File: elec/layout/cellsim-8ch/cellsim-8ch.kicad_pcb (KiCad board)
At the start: 2 copper layers, 160 parts

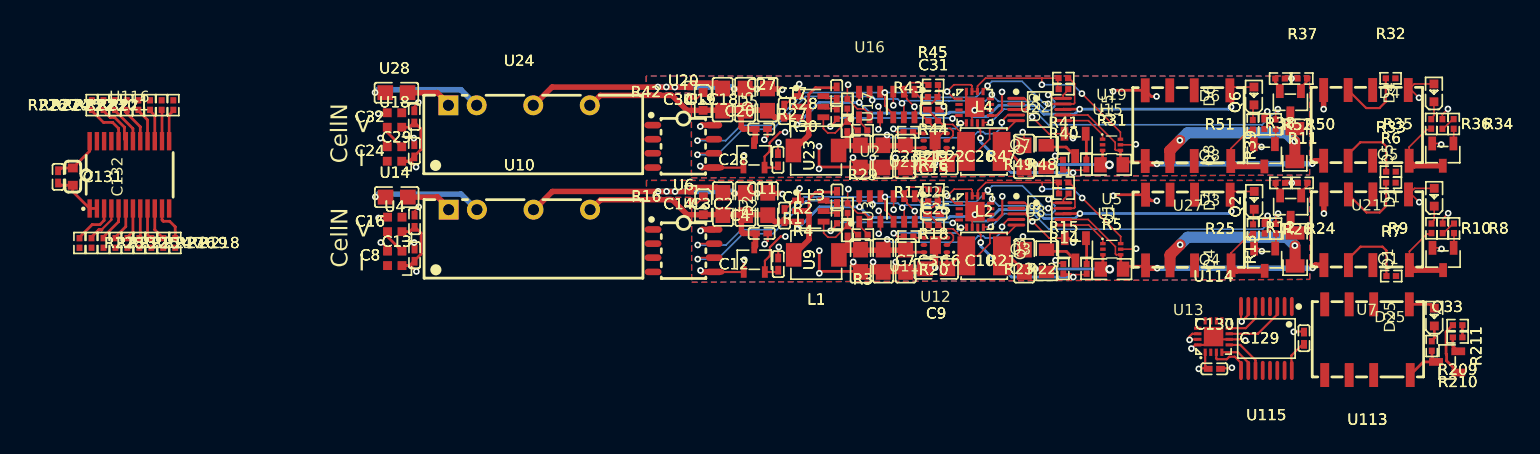
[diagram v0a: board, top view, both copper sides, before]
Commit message: remove muxes
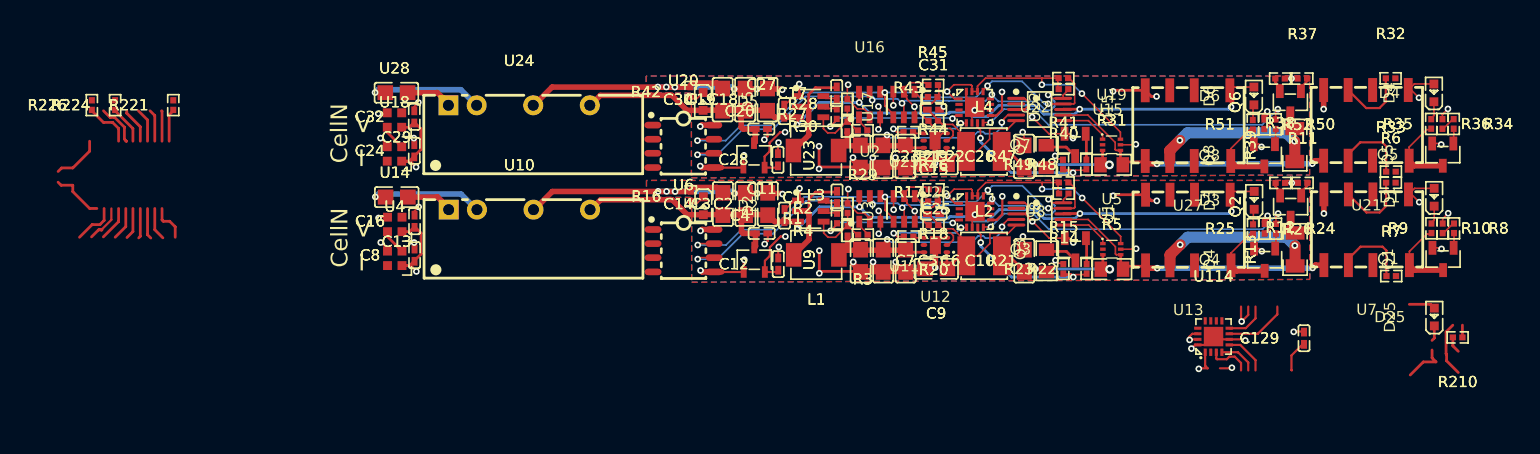
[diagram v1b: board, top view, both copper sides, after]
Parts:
- removed C130: 1µF ±10% 25V X5R, atopile:C0402-b3ef17
- removed C131: 100nF ±10% 16V X7R, atopile:C0402-b3ef17
- removed C132: 100nF ±10% 50V X7R, atopile:C0603-bd72f6
- removed Q33: , atopile:SOT-23-3_L2.9-W1.3-P1.90-LS2.4-BR-688f29
- removed R209, R212, R213, R214, R215, R216, R217, R218, R219, R220, R222, R223, R225, R227: 10kΩ ±1% 62.5mW, atopile:R0402-56259e
- removed R211, R228: 1kΩ ±1% 62.5mW, atopile:R0402-56259e
- removed U113: , lib:RELAY-SMD_HFD4-5-SR
- removed U115: , atopile:TSSOP-16_L5.0-W4.4-P0.65-LS6.4-BL-4f6acc
- removed U116: , lib:TSSOP-24_L7.8-W4.4-P0.65-LS6.4-BL
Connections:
- C10 pad 1: (no net) -> 3V3_GND
- C10 pad 2: 3V3_GND -> (no net)
- C11 pad 2: 3V3_GND -> (no net)
- C12 pad 2: 3V3_GND -> (no net)
- C129 pad 2: gnd-2 -> (no net)
- C13 pad 1: hv-4 -> hv-3
- C13 pad 2: gnd-3 -> gnd-1
- C14 pad 2: 3V3_GND -> (no net)
- C15 pad 1: hv -> hv-5
- C15 pad 2: 3V3_GND -> (no net)
- C16 pad 1: hv-3 -> hv
- C16 pad 2: gnd-1 -> gnd
- C18 pad 2: (no net) -> 3V3_GND
- C19 pad 2: (no net) -> 3V3_GND
- C2 pad 2: 3V3_GND -> (no net)
- C20 pad 2: (no net) -> 3V3_GND
- C21 pad 2: (no net) -> 3V3_GND
- C22 pad 2: (no net) -> 3V3_GND
- C23 pad 2: (no net) -> 3V3_GND
- C24 pad 1: hv-3 -> hv
- C24 pad 2: gnd-1 -> gnd
- C25 pad 1: hv-2 -> hv-4
- C25 pad 2: (no net) -> 3V3_GND
- C26 pad 2: (no net) -> 3V3_GND
- C27 pad 2: (no net) -> 3V3_GND
- C28 pad 1: (no net) -> 3V3
- C28 pad 2: (no net) -> 3V3_GND
- C29 pad 1: hv-4 -> hv-3
- C29 pad 2: gnd-3 -> gnd-1
- C3 pad 2: 3V3_GND -> (no net)
- C30 pad 2: (no net) -> 3V3_GND
- C31 pad 1: hv-2 -> hv-4
- C31 pad 2: (no net) -> 3V3_GND
- C32 pad 1: hv-3 -> hv
- C32 pad 2: gnd-1 -> gnd
- C4 pad 2: 3V3_GND -> (no net)
- C5 pad 1: hv-8 -> hv-2
- C5 pad 2: 3V3_GND -> (no net)
- C6 pad 1: hv-8 -> hv-2
- C6 pad 2: 3V3_GND -> (no net)
- C7 pad 1: hv-8 -> hv-2
- C7 pad 2: 3V3_GND -> (no net)
- C8 pad 1: hv-3 -> hv
- C8 pad 2: gnd-1 -> gnd
- C9 pad 1: hv -> hv-5
- C9 pad 2: 3V3_GND -> (no net)
- D1 pad 2: hv-3 -> hv
- D25 pad 2: hv-3 -> hv
- D4 pad 2: hv-3 -> hv
- L1 pad 2: hv-8 -> hv-2
- L2 pad 1: hv -> hv-5
- L2 pad 2: (no net) -> 3V3_GND
- L4 pad 1: hv-2 -> hv-4
- Q1 pad 2: gnd-1 -> gnd
- Q2 pad 2: cell1-gnd-5 -> cell1-gnd-3
- Q2 pad 3: cell1-gnd-1 -> cell1-gnd
- Q3 pad 2: 3V3_GND -> (no net)
- Q3 pad 3: cell1-gnd-3 -> cell1-gnd-1
- Q4 pad 2: 3V3_GND -> (no net)
- Q5 pad 2: gnd-1 -> gnd
- Q6 pad 2: cell2-gnd-5 -> cell2-gnd-1
- Q6 pad 3: cell2-gnd-1 -> cell2-gnd
- Q7 pad 2: (no net) -> 3V3_GND
- Q8 pad 2: (no net) -> 3V3_GND
- R1 pad 1: cell1-line-5 -> cell1-line
- R11 pad 1: cell1-line-9 -> cell1-line-5
- R12 pad 1: cell1-line-9 -> cell1-line-5
- R12 pad 2: cell1-gnd-5 -> cell1-gnd-3
- R13 pad 1: cell1-hv-2 -> cell1-hv-3
- R13 pad 2: cell1-gnd-1 -> cell1-gnd
- R14 pad 1: cell1-line-6 -> cell1-line-7
- R16 pad 2: 3V3_GND -> (no net)
- R17 pad 1: cell1-line-1 -> cell1-line-9
- R18 pad 2: 3V3_GND -> (no net)
- R2 pad 2: 3V3_GND -> (no net)
- R20 pad 1: hv -> hv-5
- R21 pad 1: (no net) -> 3V3_GND
- R21 pad 2: cell1-gnd-3 -> cell1-gnd-1
- R210 pad 1: line-8 -> (no net)
- R210 pad 2: gnd-1 -> gnd
- R22 pad 1: cell1-line-4 -> cell1-line-13
- R226 pad 1: i2c_mux-line-5 -> (no net)
- R23 pad 1: cell1-line-4 -> cell1-line-13
- R23 pad 2: 3V3_GND -> (no net)
- R24 pad 1: cell1-line-10 -> cell1-line-6
- R25 pad 1: cell1-line-10 -> cell1-line-6
- R25 pad 2: 3V3_GND -> (no net)
- R28 pad 2: (no net) -> 3V3_GND
- R31 pad 2: cell2-line-10 -> cell2-line-2
- R32 pad 1: cell2-gnd-2 -> cell2-gnd-4
- R32 pad 2: cell2-gnd -> cell2-gnd-2
- R33 pad 2: cell2-hv-3 -> cell2-hv
- R34 pad 1: line-6 -> cell2-line-10
- R35 pad 1: line-6 -> cell2-line-10
- R35 pad 2: gnd-1 -> gnd
- R37 pad 1: cell2-line-5 -> cell2-line-3
- R38 pad 1: cell2-line-5 -> cell2-line-3
- R38 pad 2: cell2-gnd-5 -> cell2-gnd-1
- R39 pad 1: cell2-hv -> cell2-hv-3
- R39 pad 2: cell2-gnd-1 -> cell2-gnd
- R4 pad 1: hv-8 -> hv-2
- R40 pad 1: cell2-line -> cell2-line-1
- R40 pad 2: (no net) -> 3V3
- R41 pad 1: cell2-line-8 -> cell2-line
- R41 pad 2: (no net) -> 3V3
- R42 pad 2: (no net) -> 3V3_GND
- R43 pad 1: cell2-line-1 -> cell2-line-4
- R44 pad 2: (no net) -> 3V3_GND
- R46 pad 1: hv-2 -> hv-4
- R49 pad 2: (no net) -> 3V3_GND
- R5 pad 1: (no net) -> 3V3_GND
- R5 pad 2: cell1-line -> cell1-line-1
- R50 pad 1: cell2-line-2 -> cell2-line-11
- R51 pad 1: cell2-line-2 -> cell2-line-11
- R51 pad 2: (no net) -> 3V3_GND
- R6 pad 1: cell1-gnd-2 -> cell1-gnd-5
- R6 pad 2: cell1-gnd -> cell1-gnd-4
- R7 pad 1: cell1-hv-1 -> cell1-hv-2
- R7 pad 2: cell1-hv-3 -> cell1-hv
- R8 pad 1: line -> cell1-line-3
- R9 pad 1: line -> cell1-line-3
- R9 pad 2: gnd-1 -> gnd
- U1 pad 1: cell1.adc-line-1 -> cell1.adc-line
- U1 pad 10: cell1-line-6 -> cell1-line-7
- U1 pad 2: cell1.adc-line -> cell1.adc-line-1
- U1 pad 3: 3V3_GND -> (no net)
- U1 pad 4: hv-8 -> hv-2
- U1 pad 5: hv -> hv-5
- U1 pad 6: cell1-line-3 -> cell1-line-2
- U1 pad 7: cell1-line -> cell1-line-1
- U10 pad 1: hv-4 -> hv-3
- U10 pad 2: gnd-3 -> gnd-1
- U10 pad 4: 3V3_GND -> (no net)
- U11 pad 2: 3V3_GND -> (no net)
- U11 pad 5: cell1-line-6 -> cell1-line-7
- U11 pad 6: 3V3_GND -> (no net)
- U114 pad 10: gpio_mux.gpio_expander-net-2 -> (no net)
- U114 pad 11: gpio_mux.gpio_expander-INT -> (no net)
- U114 pad 12: line-1 -> (no net)
- U114 pad 13: line-3 -> (no net)
- U114 pad 17: gnd-2 -> (no net)
- U114 pad 2: gpio_mux.gpio_expander-net-1 -> (no net)
- U114 pad 3: S2 -> (no net)
- U114 pad 4: S1 -> (no net)
- U114 pad 5: S0 -> (no net)
- U114 pad 6: gnd-2 -> (no net)
- U114 pad 8: Eh -> (no net)
- U114 pad 9: gpio_mux.gpio_expander-net -> (no net)
- U12 pad 1: hv -> hv-5
- U12 pad 3: 3V3_GND -> (no net)
- U12 pad 6: hv-8 -> hv-2
- U12 pad 7: 3V3_GND -> (no net)
- U13 pad 3: cell1-gnd-5 -> cell1-gnd-3
- U13 pad 4: 3V3_GND -> (no net)
- U13 pad 5: cell1-line -> cell1-line-1
- U13 pad 6: cell1-hv-2 -> cell1-hv-3
- U14 pad 1: hv-3 -> hv
- U14 pad 2: line-5 -> line
- U14 pad 3: gnd-1 -> gnd
- U14 pad 4: cell1-line-2 -> cell1-line-10
- U15 pad 1: cell2.adc-line -> cell2.adc-line-1
- U15 pad 10: cell2-line -> cell2-line-1
- U15 pad 2: cell2.adc-line-1 -> cell2.adc-line
- U15 pad 3: (no net) -> 3V3_GND
- U15 pad 5: hv-2 -> hv-4
- U15 pad 6: cell2-line-4 -> cell2-line-12
- U15 pad 7: cell2-line-10 -> cell2-line-2
- U15 pad 9: cell2-line-8 -> cell2-line
- U16 pad 2: (no net) -> 3V3_GND
- U16 pad 3: (no net) -> 3V3
- U16 pad 4: cell2-line-8 -> cell2-line
- U16 pad 5: cell2-line -> cell2-line-1
- U17 pad 1: (no net) -> 3V3_GND
- U18 pad 1: hv-3 -> hv
- U18 pad 2: cell2-line-3 -> cell2-line-8
- U18 pad 3: gnd-1 -> gnd
- U18 pad 4: line-5 -> line
- U19 pad 1: cell2-line-4 -> cell2-line-12
- U19 pad 2: (no net) -> 3V3_GND
- U19 pad 4: cell2-line-10 -> cell2-line-2
- U19 pad 5: (no net) -> 3V3_GND
- U19 pad 6: (no net) -> 3V3
- U2 pad 2: 3V3_GND -> (no net)
- U2 pad 5: cell1-line-6 -> cell1-line-7
- U20 pad 2: line-4 -> cell2-line-13
- U20 pad 3: line-9 -> cell2-line-7
- U20 pad 4: cell2-gnd-4 -> cell2-gnd-5
- U20 pad 5: (no net) -> 3V3_GND
- U20 pad 6: cell2-line -> cell2-line-1
- U20 pad 7: cell2-line-8 -> cell2-line
- U20 pad 8: (no net) -> 3V3
- U21 pad 1: hv-3 -> hv
- U21 pad 3: cell2-gnd-2 -> cell2-gnd-4
- U21 pad 4: (no net) -> 3V3_GND
- U21 pad 5: cell2-line-10 -> cell2-line-2
- U22 pad 1: (no net) -> 3V3
- U22 pad 10: cell2.gpio-net-2 -> cell2.gpio-net
- U22 pad 12: cell2-line -> cell2-line-1
- U22 pad 13: cell2-line-8 -> cell2-line
- U22 pad 14: (no net) -> 3V3
- U22 pad 15: (no net) -> 3V3
- U22 pad 16: (no net) -> 3V3_GND
- U22 pad 17: (no net) -> 3V3_GND
- U22 pad 3: cell2.gpio-net -> cell2.gpio-net-2
- U22 pad 5: cell2-line-1 -> cell2-line-4
- U22 pad 6: (no net) -> 3V3_GND
- U22 pad 8: cell2-line-2 -> cell2-line-11
- U22 pad 9: cell2-line-5 -> cell2-line-3
- U23 pad 1: (no net) -> 3V3_GND
- U23 pad 2: (no net) -> 3V3
- U24 pad 1: hv-4 -> hv-3
- U24 pad 2: gnd-3 -> gnd-1
- U24 pad 4: (no net) -> 3V3_GND
- U25 pad 2: (no net) -> 3V3_GND
- U25 pad 3: (no net) -> 3V3
- U25 pad 4: cell2-line-8 -> cell2-line
- U25 pad 5: cell2-line -> cell2-line-1
- U25 pad 6: (no net) -> 3V3_GND
- U26 pad 1: hv-2 -> hv-4
- U26 pad 3: (no net) -> 3V3_GND
- U26 pad 7: (no net) -> 3V3_GND
- U27 pad 3: cell2-gnd-5 -> cell2-gnd-1
- U27 pad 4: (no net) -> 3V3_GND
- U27 pad 5: cell2-line-10 -> cell2-line-2
- U27 pad 6: cell2-hv -> cell2-hv-3
- U28 pad 1: hv-3 -> hv
- U28 pad 2: cell2-line-7 -> cell2-line-5
- U28 pad 3: gnd-1 -> gnd
- U28 pad 4: cell2-line-3 -> cell2-line-8
- U3 pad 1: 3V3_GND -> (no net)
- U4 pad 1: hv-3 -> hv
- U4 pad 2: cell1-line-2 -> cell1-line-10
- U4 pad 3: gnd-1 -> gnd
- U4 pad 4: cell1-line-7 -> cell1-line-11
- U5 pad 1: cell1-line-3 -> cell1-line-2
- U5 pad 2: 3V3_GND -> (no net)
- U5 pad 3: (no net) -> 3V3_GND
- U5 pad 4: cell1-line -> cell1-line-1
- U5 pad 5: 3V3_GND -> (no net)
- U6 pad 1: cell1-hv -> cell1-hv-1
- U6 pad 2: line-2 -> cell1-line-4
- U6 pad 3: line-7 -> cell1-line-12
- U6 pad 4: cell1-gnd-4 -> cell1-gnd-2
- U6 pad 5: 3V3_GND -> (no net)
- U6 pad 6: cell1-line-6 -> cell1-line-7
- U7 pad 1: hv-3 -> hv
- U7 pad 3: cell1-gnd-2 -> cell1-gnd-5
- U7 pad 4: 3V3_GND -> (no net)
- U7 pad 5: cell1-line -> cell1-line-1
- U7 pad 6: cell1-hv-1 -> cell1-hv-2
- U8 pad 10: cell1.gpio-net-2 -> cell1.gpio-net-1
- U8 pad 12: cell1-line-6 -> cell1-line-7
- U8 pad 16: 3V3_GND -> (no net)
- U8 pad 17: 3V3_GND -> (no net)
- U8 pad 2: cell1.gpio-net-1 -> cell1.gpio-net
- U8 pad 3: cell1.gpio-net -> cell1.gpio-net-2
- U8 pad 4: cell1-line-5 -> cell1-line
- U8 pad 5: cell1-line-1 -> cell1-line-9
- U8 pad 6: 3V3_GND -> (no net)
- U8 pad 7: cell1-line-4 -> cell1-line-13
- U8 pad 8: cell1-line-10 -> cell1-line-6
- U8 pad 9: cell1-line-9 -> cell1-line-5
- U9 pad 1: 3V3_GND -> (no net)
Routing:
- net cell1.adc-line-1: track 103.3 -> 5.43 mm, vias 29 -> 2
- net cell1.adc-line: track 5.43 -> 103.3 mm, vias 2 -> 29
- net (no net): track 186.3 -> 256.9 mm, vias 37 -> 40
- net cell2-line-1: track 7.72 -> 77.6 mm, vias 2 -> 13
- net cell1-line-7: track 0.00 -> 43.5 mm, vias 0 -> 5
- net cell2-line-8: track 44.5 -> 2.29 mm, vias 4 -> 0
- net cell2-line: track 77.6 -> 44.5 mm, vias 13 -> 4
- net cell2-line-5: track 30.5 -> 0.00 mm, vias 2 -> 0
- net cell2-line-11: track 0.00 -> 30.4 mm, vias 0 -> 2
- net cell2-line-3: track 2.29 -> 30.5 mm, vias 0 -> 2
- net cell1-line-10: track 30.4 -> 2.29 mm, vias 2 -> 0
- net cell2-line-10: track 26.6 -> 1.44 mm, vias 2 -> 0
- net hv-8: track 24.3 -> 0.00 mm, vias 2 -> 0
- net cell1-line-9: track 30.5 -> 7.72 mm
- net gnd-3: track 21.6 -> 0.00 mm, vias 2 -> 0
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
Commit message: update cell.ato
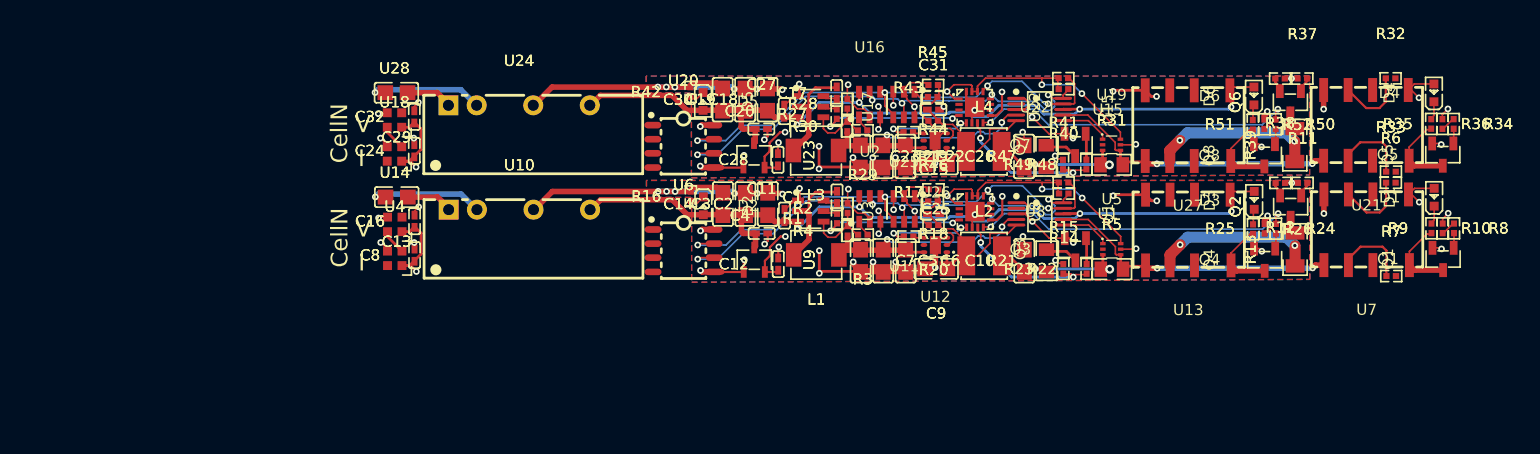
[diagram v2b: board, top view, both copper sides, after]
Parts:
- removed C129: 100nF ±10% 16V X7R, atopile:C0402-b3ef17
- removed D25: , atopile:LED0603-RD-c81ffb
- removed R210: 1kΩ ±1% 62.5mW, atopile:R0402-56259e
- removed R221, R224, R226: 10kΩ ±1% 62.5mW, atopile:R0402-56259e
- removed U114: , atopile:QFN-16_L3.0-W3.0-P0.50-BL-EP1.7-3a4c56
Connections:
- C11 pad 1: 5V -> (no net)
- C13 pad 1: hv-3 -> hv
- C14 pad 1: 5V -> (no net)
- C16 pad 1: hv -> hv-3
- C18 pad 1: (no net) -> 5V
- C19 pad 1: (no net) -> 5V
- C2 pad 1: 5V -> (no net)
- C20 pad 1: (no net) -> 5V
- C21 pad 1: hv-1 -> hv-2
- C22 pad 1: hv-1 -> hv-2
- C23 pad 1: hv-1 -> hv-2
- C24 pad 1: hv -> hv-3
- C25 pad 1: hv-4 -> hv-6
- C26 pad 1: hv-6 -> hv-1
- C27 pad 1: (no net) -> 5V
- C29 pad 1: hv-3 -> hv
- C3 pad 1: 5V -> (no net)
- C30 pad 1: (no net) -> 5V
- C31 pad 1: hv-4 -> hv-6
- C32 pad 1: hv -> hv-3
- C4 pad 1: 5V -> (no net)
- C5 pad 1: hv-2 -> hv-4
- C6 pad 1: hv-2 -> hv-4
- C7 pad 1: hv-2 -> hv-4
- C8 pad 1: hv -> hv-3
- D1 pad 2: hv -> hv-3
- D2 pad 2: 5V -> (no net)
- D3 pad 2: 5V -> (no net)
- D4 pad 2: hv -> hv-3
- D5 pad 2: (no net) -> 5V
- D6 pad 2: (no net) -> 5V
- L1 pad 2: hv-2 -> hv-4
- L3 pad 2: hv-1 -> hv-2
- L4 pad 1: hv-4 -> hv-6
- L4 pad 2: hv-6 -> hv-1
- Q2 pad 2: cell1-gnd-3 -> cell1-gnd-5
- Q2 pad 3: cell1-gnd -> cell1-gnd-1
- Q3 pad 3: cell1-gnd-1 -> cell1-gnd
- Q6 pad 2: cell2-gnd-1 -> cell2-gnd-5
- Q6 pad 3: cell2-gnd -> cell2-gnd-1
- Q7 pad 3: cell2-gnd-3 -> cell2-gnd
- R1 pad 1: cell1-line -> cell1-line-2
- R11 pad 1: cell1-line-5 -> cell1-line-8
- R12 pad 1: cell1-line-5 -> cell1-line-8
- R12 pad 2: cell1-gnd-3 -> cell1-gnd-5
- R13 pad 1: cell1-hv-3 -> cell1-hv-2
- R13 pad 2: cell1-gnd -> cell1-gnd-1
- R14 pad 1: cell1-line-7 -> cell1-line-3
- R15 pad 1: cell1-line-8 -> cell1-line-6
- R17 pad 1: cell1-line-9 -> cell1-line
- R21 pad 2: cell1-gnd-1 -> cell1-gnd
- R22 pad 1: cell1-line-13 -> cell1-line-1
- R23 pad 1: cell1-line-13 -> cell1-line-1
- R24 pad 1: cell1-line-6 -> cell1-line-5
- R25 pad 1: cell1-line-6 -> cell1-line-5
- R27 pad 1: cell2-line-6 -> cell2-line-10
- R30 pad 1: hv-1 -> hv-2
- R31 pad 1: hv-6 -> hv-1
- R31 pad 2: cell2-line-2 -> cell2-line-4
- R32 pad 1: cell2-gnd-4 -> cell2-gnd-2
- R32 pad 2: cell2-gnd-2 -> cell2-gnd-3
- R33 pad 2: cell2-hv -> cell2-hv-3
- R34 pad 1: cell2-line-10 -> cell2-line-7
- R35 pad 1: cell2-line-10 -> cell2-line-7
- R37 pad 1: cell2-line-3 -> cell2-line
- R38 pad 1: cell2-line-3 -> cell2-line
- R38 pad 2: cell2-gnd-1 -> cell2-gnd-5
- R39 pad 1: cell2-hv-3 -> cell2-hv-1
- R39 pad 2: cell2-gnd -> cell2-gnd-1
- R4 pad 1: hv-2 -> hv-4
- R40 pad 1: cell2-line-1 -> cell2-line-9
- R41 pad 1: cell2-line -> cell2-line-11
- R43 pad 1: cell2-line-4 -> cell2-line-6
- R46 pad 1: hv-4 -> hv-6
- R47 pad 1: hv-6 -> hv-1
- R47 pad 2: cell2-gnd-3 -> cell2-gnd
- R48 pad 1: cell2-line-9 -> cell2-line-13
- R49 pad 1: cell2-line-9 -> cell2-line-13
- R5 pad 2: cell1-line-1 -> cell1-line-13
- R50 pad 1: cell2-line-11 -> cell2-line-2
- R51 pad 1: cell2-line-11 -> cell2-line-2
- R6 pad 1: cell1-gnd-5 -> cell1-gnd-3
- R7 pad 1: cell1-hv-2 -> cell1-hv
- R7 pad 2: cell1-hv -> cell1-hv-3
- R8 pad 1: cell1-line-3 -> cell1-line-11
- R9 pad 1: cell1-line-3 -> cell1-line-11
- U1 pad 10: cell1-line-7 -> cell1-line-3
- U1 pad 4: hv-2 -> hv-4
- U1 pad 6: cell1-line-2 -> cell1-line-10
- U1 pad 7: cell1-line-1 -> cell1-line-13
- U1 pad 8: 5V -> (no net)
- U1 pad 9: cell1-line-8 -> cell1-line-6
- U10 pad 1: hv-3 -> hv
- U10 pad 6: 5V -> (no net)
- U11 pad 4: cell1-line-8 -> cell1-line-6
- U11 pad 5: cell1-line-7 -> cell1-line-3
- U12 pad 6: hv-2 -> hv-4
- U13 pad 1: 5V -> (no net)
- U13 pad 3: cell1-gnd-3 -> cell1-gnd-5
- U13 pad 5: cell1-line-1 -> cell1-line-13
- U13 pad 6: cell1-hv-3 -> cell1-hv-2
- U14 pad 1: hv -> hv-3
- U14 pad 4: cell1-line-10 -> cell1-line-4
- U15 pad 1: cell2.adc-line-1 -> cell2.adc-line
- U15 pad 10: cell2-line-1 -> cell2-line-9
- U15 pad 2: cell2.adc-line -> cell2.adc-line-1
- U15 pad 4: hv-1 -> hv-2
- U15 pad 5: hv-4 -> hv-6
- U15 pad 6: cell2-line-12 -> cell2-line-3
- U15 pad 7: cell2-line-2 -> cell2-line-4
- U15 pad 8: (no net) -> 5V
- U15 pad 9: cell2-line -> cell2-line-11
- U16 pad 4: cell2-line -> cell2-line-11
- U16 pad 5: cell2-line-1 -> cell2-line-9
- U16 pad 6: (no net) -> 5V
- U17 pad 3: (no net) -> 5V
- U18 pad 1: hv -> hv-3
- U18 pad 2: cell2-line-8 -> cell2-line-1
- U19 pad 1: cell2-line-12 -> cell2-line-3
- U19 pad 3: hv-6 -> hv-1
- U19 pad 4: cell2-line-2 -> cell2-line-4
- U2 pad 4: cell1-line-8 -> cell1-line-6
- U2 pad 5: cell1-line-7 -> cell1-line-3
- U2 pad 6: 5V -> (no net)
- U20 pad 1: cell2-hv-1 -> cell2-hv
- U20 pad 2: cell2-line-13 -> cell2-line-8
- U20 pad 3: cell2-line-7 -> cell2-line-5
- U20 pad 4: cell2-gnd-5 -> cell2-gnd-4
- U20 pad 6: cell2-line-1 -> cell2-line-9
- U20 pad 7: cell2-line -> cell2-line-11
- U21 pad 1: hv -> hv-3
- U21 pad 3: cell2-gnd-4 -> cell2-gnd-2
- U21 pad 5: cell2-line-2 -> cell2-line-4
- U22 pad 10: cell2.gpio-net -> cell2.gpio-net-1
- U22 pad 12: cell2-line-1 -> cell2-line-9
- U22 pad 13: cell2-line -> cell2-line-11
- U22 pad 2: cell2.gpio-net-1 -> cell2.gpio-net
- U22 pad 4: cell2-line-6 -> cell2-line-10
- U22 pad 5: cell2-line-4 -> cell2-line-6
- U22 pad 7: cell2-line-9 -> cell2-line-13
- U22 pad 8: cell2-line-11 -> cell2-line-2
- U22 pad 9: cell2-line-3 -> cell2-line
- U23 pad 3: (no net) -> 5V
- U24 pad 1: hv-3 -> hv
- U24 pad 6: (no net) -> 5V
- U25 pad 4: cell2-line -> cell2-line-11
- U25 pad 5: cell2-line-1 -> cell2-line-9
- U26 pad 1: hv-4 -> hv-6
- U26 pad 6: hv-1 -> hv-2
- U27 pad 1: (no net) -> 5V
- U27 pad 3: cell2-gnd-1 -> cell2-gnd-5
- U27 pad 5: cell2-line-2 -> cell2-line-4
- U27 pad 6: cell2-hv-3 -> cell2-hv-1
- U28 pad 1: hv -> hv-3
- U28 pad 2: cell2-line-5 -> cell2-line-12
- U28 pad 4: cell2-line-8 -> cell2-line-1
- U3 pad 3: 5V -> (no net)
- U4 pad 1: hv -> hv-3
- U4 pad 2: cell1-line-10 -> cell1-line-4
- U4 pad 4: cell1-line-11 -> cell1-line-7
- U5 pad 1: cell1-line-2 -> cell1-line-10
- U5 pad 4: cell1-line-1 -> cell1-line-13
- U6 pad 2: cell1-line-4 -> cell1-line-9
- U6 pad 6: cell1-line-7 -> cell1-line-3
- U6 pad 7: cell1-line-8 -> cell1-line-6
- U7 pad 1: hv -> hv-3
- U7 pad 3: cell1-gnd-5 -> cell1-gnd-3
- U7 pad 5: cell1-line-1 -> cell1-line-13
- U7 pad 6: cell1-hv-2 -> cell1-hv
- U8 pad 12: cell1-line-7 -> cell1-line-3
- U8 pad 13: cell1-line-8 -> cell1-line-6
- U8 pad 4: cell1-line -> cell1-line-2
- U8 pad 5: cell1-line-9 -> cell1-line
- U8 pad 7: cell1-line-13 -> cell1-line-1
- U8 pad 8: cell1-line-6 -> cell1-line-5
- U8 pad 9: cell1-line-5 -> cell1-line-8
- U9 pad 3: 5V -> (no net)
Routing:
- net 3V3_GND: track 0.00 -> 109.3 mm, vias 0 -> 30
- net (no net): track 256.9 -> 152.4 mm, vias 40 -> 11
- net 5V: track 75.3 -> 0.00 mm, vias 4 -> 0
- net cell2-line-1: track 77.6 -> 2.29 mm, vias 13 -> 0
- net cell1-line-7: track 43.5 -> 0.00 mm, vias 5 -> 0
- net cell1-line-3: track 1.44 -> 43.5 mm, vias 0 -> 5
- net 3V3: track 34.0 -> 68.1 mm, vias 8 -> 16
- net cell2-line-9: track 13.5 -> 43.5 mm, vias 2 -> 5
- net cell2-line-3: track 30.5 -> 4.47 mm, vias 2 -> 0
- net cell2-line-4: track 7.72 -> 26.6 mm
- net hv: track 25.3 -> 8.67 mm, vias 4 -> 0
- net cell2-hv-3: track 15.0 -> 0.00 mm, vias 2 -> 0
- net cell2-hv-1: track 0.00 -> 15.0 mm, vias 0 -> 2
- net cell1-hv-3: track 15.0 -> 0.00 mm, vias 2 -> 0
- net hv-3: track 8.67 -> 22.9 mm, vias 0 -> 4
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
